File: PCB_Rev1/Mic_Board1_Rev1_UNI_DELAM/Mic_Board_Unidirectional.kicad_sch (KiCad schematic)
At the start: 29 parts, among them J2 532610771, J3 S2B-ZR-SM4A-TF_LF__SN_, U1 OPA1671IDBVR

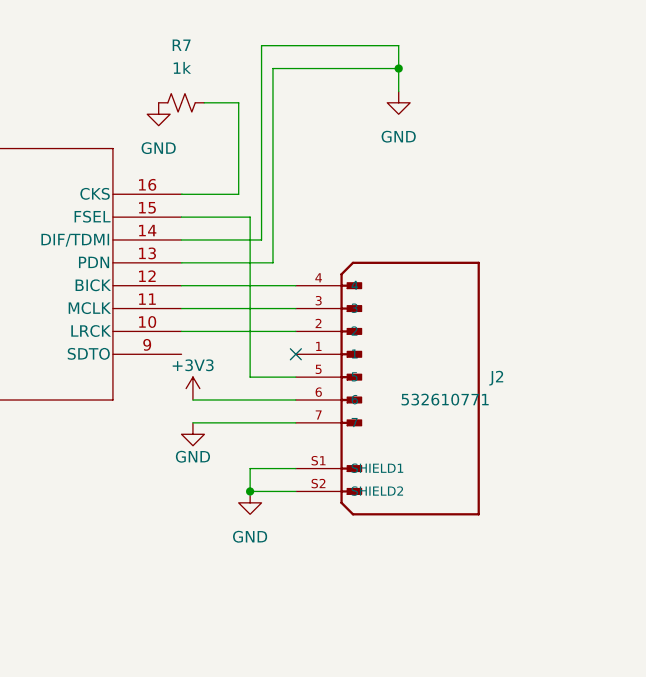
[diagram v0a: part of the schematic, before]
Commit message: Connections Adjustments
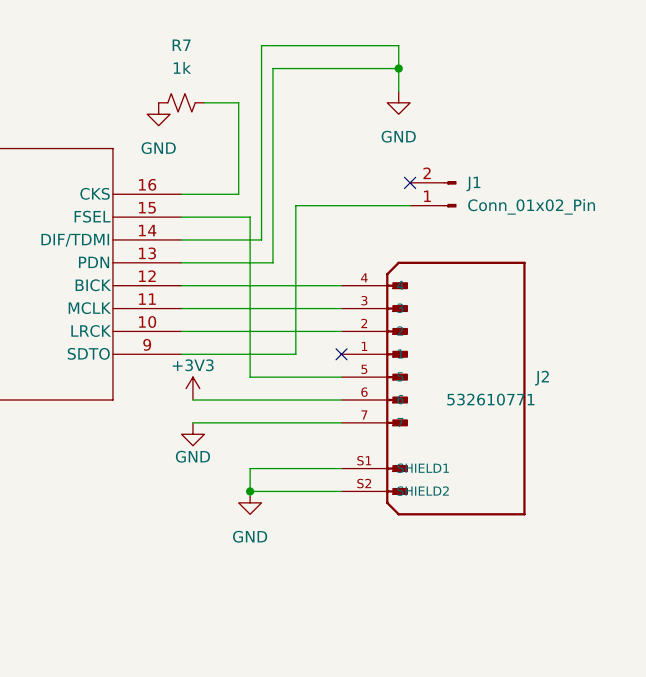
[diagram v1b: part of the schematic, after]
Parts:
- added J1: Conn_01x02_Pin, Connector_PinHeader_2.54mm:PinHeader_1x02_P2.54mm_Vertical, symbol Connector:Conn_01x02_Pin
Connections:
- net at U2.9 (SDTO): now also J1.1 (Pin_1)
- no-connect marks 1 -> 2
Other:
- moved on the sheet: J2
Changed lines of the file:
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@@
 	)
 	(no_connect
-		(at 247.65 101.6)
+		(at 260.35 82.55)
+	)
+	(no_connect
+		(at 252.73 101.6)
 	)
 	(wire
@@
 	(wire
 		(pts
+			(xy 247.65 85.09) (xy 260.35 85.09)
+		)
+		(stroke
+			(width 0)
+			(type default)
+		)
+	)
+	(wire
+		(pts
 			(xy 176.53 83.82) (xy 184.15 83.82)
 		)
@@
 	(wire
 		(pts
-			(xy 236.22 106.68) (xy 247.65 106.68)
+			(xy 236.22 106.68) (xy 252.73 106.68)
 		)
 		(stroke
@@
 	(wire
 		(pts
+			(xy 234.95 101.6) (xy 247.65 101.6)
+		)
+		(stroke
+			(width 0)
+			(type default)
+		)
+	)
+	(wire
+		(pts
 			(xy 40.64 86.36) (xy 44.45 86.36)
 		)
@@
 	(wire
 		(pts
-			(xy 247.65 93.98) (xy 234.95 93.98)
+			(xy 252.73 93.98) (xy 234.95 93.98)
 		)
 		(stroke
@@
 	(wire
 		(pts
-			(xy 236.22 109.22) (xy 247.65 109.22)
-		)
-		(stroke
-			(width 0)
-			(type default)
-		)
-	)
-	(wire
-		(pts
-			(xy 242.57 104.14) (xy 247.65 104.14)
+			(xy 236.22 109.22) (xy 252.73 109.22)
+		)
+		(stroke
+			(width 0)
+			(type default)
+		)
+	)
+	(wire
+		(pts
+			(xy 242.57 104.14) (xy 252.73 104.14)
 		)
 		(stroke
@@
 	(wire
 		(pts
-			(xy 247.65 114.3) (xy 242.57 114.3)
+			(xy 252.73 114.3) (xy 242.57 114.3)
 		)
 		(stroke
@@
 	(wire
 		(pts
-			(xy 242.57 116.84) (xy 247.65 116.84)
+			(xy 242.57 116.84) (xy 252.73 116.84)
 		)
 		(stroke
@@
 	(wire
 		(pts
-			(xy 247.65 99.06) (xy 234.95 99.06)
+			(xy 252.73 99.06) (xy 234.95 99.06)
 		)
 		(stroke
@@
 	(wire
 		(pts
+			(xy 247.65 101.6) (xy 247.65 85.09)
+		)
+		(stroke
+			(width 0)
+			(type default)
+		)
+	)
+	(wire
+		(pts
 			(xy 40.64 83.82) (xy 67.31 83.82)
 		)
@@
 	(wire
 		(pts
-			(xy 247.65 96.52) (xy 234.95 96.52)
+			(xy 252.73 96.52) (xy 234.95 96.52)
 		)
 		(stroke
@@
 	)
 	(symbol
+		(lib_id "Connector:Conn_01x02_Pin")
+		(at 265.43 85.09 180)
+		(unit 1)
+		(exclude_from_sim no)
+		(in_bom yes)
+		(on_board yes)
+		(dnp no)
+		(fields_autoplaced yes)
+		(property "Reference" "J1"
+			(at 266.7 82.5499 0)
+			(effects
+				(font
+					(size 1.27 1.27)
+				)
+				(justify right)
+			)
+		)
+		(property "Value" "Conn_01x02_Pin"
+			(at 266.7 85.0899 0)
+			(effects
+				(font
+					(size 1.27 1.27)
+				)
+				(justify right)
+			)
+		)
+		(property "Footprint" "Connector_PinHeader_2.54mm:PinHeader_1x02_P2.54mm_Vertical"
+			(at 265.43 85.09 0)
+			(effects
+				(font
+					(size 1.27 1.27)
+				)
+				(hide yes)
+			)
+		)
+		(property "Datasheet" "~"
+			(at 265.43 85.09 0)
+			(effects
+				(font
+					(size 1.27 1.27)
+				)
+				(hide yes)
+			)
+		)
+		(property "Description" "Generic connector, single row, 01x02, script generated"
+			(at 265.43 85.09 0)
+			(effects
+				(font
+					(size 1.27 1.27)
+				)
+				(hide yes)
+			)
+		)
+		(pin "2"
+		)
+		(pin "1"
+		)
+		(instances
+			(project ""
+				(path "/1178ae07-c232-447f-a548-6d4f89d4abce"
+					(reference "J1")
+					(unit 1)
+				)
+			)
+		)
+	)
+	(symbol
 		(lib_id "532610771:532610771")
-		(at 260.35 104.14 0)
+		(at 265.43 104.14 0)
 		(unit 1)
 		(exclude_from_sim no)
@@
 		(dnp no)
 		(property "Reference" "J2"
-			(at 269.24 104.14 0)
+			(at 274.32 104.14 0)
 			(effects
 				(font
@@
 		)
 		(property "Value" "532610771"
-			(at 269.24 106.68 0)
+			(at 274.32 106.68 0)
 			(effects
 				(font
@@
 		)
 		(property "Footprint" "Footprints:MOLEX_connector"
-			(at 260.35 104.14 0)
+			(at 265.43 104.14 0)
 			(effects
 				(font
@@
 		)
 		(property "Datasheet" ""
-			(at 260.35 104.14 0)
+			(at 265.43 104.14 0)
 			(effects
 				(font
@@
 		)
 		(property "Description" "\nPicoblade Connector, 7 Circuit Single Row, Right Angle Surface Mount SMT PCB\n"
-			(at 260.35 104.14 0)
+			(at 265.43 104.14 0)
 			(effects
 				(font
@@
 		)
 		(property "DigiKey_Part_Number" "WM7625TR-ND"
-			(at 260.35 104.14 0)
+			(at 265.43 104.14 0)
 			(effects
 				(font
@@
 		)
 		(property "MF" "Molex"
-			(at 260.35 104.14 0)
+			(at 265.43 104.14 0)
 			(effects
 				(font
@@
 		)
 		(property "MAXIMUM_PACKAGE_HEIGHT" "3.4 mm"
-			(at 260.35 104.14 0)
+			(at 265.43 104.14 0)
 			(effects
 				(font
@@
 		)
 		(property "Package" "None"
-			(at 260.35 104.14 0)
+			(at 265.43 104.14 0)
 			(effects
 				(font
@@
 		)
 		(property "Check_prices" "https://www.snapeda.com/parts/0532610771/Molex/view-part/?ref=eda"
-			(at 260.35 104.14 0)
+			(at 265.43 104.14 0)
 			(effects
 				(font
@@
 		)
 		(property "STANDARD" "Manufacturer Recommendations"
-			(at 260.35 104.14 0)
+			(at 265.43 104.14 0)
 			(effects
 				(font
@@
 		)
 		(property "PARTREV" "J"
-			(at 260.35 104.14 0)
+			(at 265.43 104.14 0)
 			(effects
 				(font
@@
 		)
 		(property "SnapEDA_Link" "https://www.snapeda.com/parts/0532610771/Molex/view-part/?ref=snap"
-			(at 260.35 104.14 0)
+			(at 265.43 104.14 0)
 			(effects
 				(font
@@
 		)
 		(property "MP" "0532610771"
-			(at 260.35 104.14 0)
+			(at 265.43 104.14 0)
 			(effects
 				(font
@@
 		)
 		(property "Purchase-URL" "https://www.snapeda.com/api/url_track_click_mouser/?unipart_id=577144&manufacturer=Molex&part_name=0532610771&search_term=None"
-			(at 260.35 104.14 0)
+			(at 265.43 104.14 0)
 			(effects
 				(font
@@
 		)
 		(property "MANUFACTURER" "Molex"
-			(at 260.35 104.14 0)
-			(effects
-				(font
+			(at 265.43 104.14 0)
+			(effects
+				(font
